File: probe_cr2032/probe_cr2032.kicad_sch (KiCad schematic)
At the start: 20 parts, among them J0 R0, U1 MCP73831-2-OT, U2 LTC3525-5, U3 MCP102-240D

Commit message: - add lasr fix
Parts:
- removed 5V1, 5V2, GND1, GND2: (no value), TestPoint:TestPoint_Pad_D1.5mm, symbol Connector:TestPoint
- removed C3: C1uF, Resistor_SMD:R_0603_1608Metric, symbol Device:C
- removed C4: C22uF, Resistor_SMD:R_0603_1608Metric, symbol Device:C
- removed J0: R0, Resistor_SMD:R_0201_0603Metric, symbol Device:R
- removed L1: 10UH, Inductor_SMD:L_Vishay_IFSC-1515AH_4x4x1.8mm, symbol Device:L
- removed U2: LTC3525-5, Package_TO_SOT_SMD:SOT-363_SC-70-6, symbol Regulator_Switching:LTC3525-5
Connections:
- net +5V: no longer names the net of C1.1, POW1.2 (A), U1.4 (VDD), USBC1.A9 (VBUS), USBC1.B9 (VBUS)

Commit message: - add new power version
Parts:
- removed U3: MCP102-240D, Package_TO_SOT_SMD:SOT-23, symbol Power_Supervisor:MCP100-270D
- added J?: Conn_01x03, Connector_Molex:Molex_CLIK-Mate_502386-0370_1x03-1MP_P1.25mm_Horizontal, symbol Connector_Generic:Conn_01x03
- added U?: APX809-23SAG-7, Package_TO_SOT_SMD:SOT-23, symbol 2025-03-20_10-07-06:APX809-23SAG-7
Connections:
- net GND: now also J?.3 (Pin_3), U?.1 (GND)
- net at C2.1, U1.3 (VBAT): now also J?.1 (Pin_1), U?.3 (VCC)
- net at LOW1.1: now also J?.2 (Pin_2), U?.2 (*RESET)
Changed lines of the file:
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@@
   (junction (at 156.21 72.39) (diameter 0) (color 0 0 0 0)
   )
+  (junction (at 204.47 85.09) (diameter 0) (color 0 0 0 0)
+  )
   (junction (at 111.76 67.31) (diameter 0) (color 0 0 0 0)
   )
@@
     (stroke (width 0) (type default) (color 0 0 0 0))
   )
-  (wire (pts (xy 186.69 95.25) (xy 186.69 97.79))
+  (wire (pts (xy 227.33 80.01) (xy 227.33 64.77))
+    (stroke (width 0) (type default) (color 0 0 0 0))
+  )
+  (wire (pts (xy 186.69 147.32) (xy 186.69 149.86))
     (stroke (width 0) (type default) (color 0 0 0 0))
   )
@@
     (stroke (width 0) (type default) (color 0 0 0 0))
   )
+  (wire (pts (xy 227.33 82.55) (xy 219.71 82.55))
+    (stroke (width 0) (type default) (color 0 0 0 0))
+  )
   (wire (pts (xy 60.96 67.31) (xy 60.96 109.22))
     (stroke (width 0) (type default) (color 0 0 0 0))
@@
     (stroke (width 0) (type default) (color 0 0 0 0))
   )
-  (wire (pts (xy 186.69 72.39) (xy 186.69 74.93))
+  (wire (pts (xy 186.69 72.39) (xy 186.69 86.36))
     (stroke (width 0) (type default) (color 0 0 0 0))
   )
@@
     (stroke (width 0) (type default) (color 0 0 0 0))
   )
+  (wire (pts (xy 227.33 64.77) (xy 165.1 64.77))
+    (stroke (width 0) (type default) (color 0 0 0 0))
+  )
   (wire (pts (xy 165.1 72.39) (xy 186.69 72.39))
     (stroke (width 0) (type default) (color 0 0 0 0))
@@
     (stroke (width 0) (type default) (color 0 0 0 0))
   )
+  (wire (pts (xy 189.23 86.36) (xy 189.23 85.09))
+    (stroke (width 0) (type default) (color 0 0 0 0))
+  )
+  (wire (pts (xy 226.06 85.09) (xy 226.06 88.9))
+    (stroke (width 0) (type default) (color 0 0 0 0))
+  )
+  (wire (pts (xy 204.47 85.09) (xy 219.71 85.09))
+    (stroke (width 0) (type default) (color 0 0 0 0))
+  )
+  (wire (pts (xy 189.23 85.09) (xy 204.47 85.09))
+    (stroke (width 0) (type default) (color 0 0 0 0))
+  )
+  (wire (pts (xy 227.33 85.09) (xy 226.06 85.09))
+    (stroke (width 0) (type default) (color 0 0 0 0))
+  )
   (wire (pts (xy 149.86 93.98) (xy 149.86 97.79))
     (stroke (width 0) (type default) (color 0 0 0 0))
   )
+  (wire (pts (xy 165.1 64.77) (xy 165.1 72.39))
+    (stroke (width 0) (type default) (color 0 0 0 0))
+  )
   (wire (pts (xy 135.89 77.47) (xy 139.7 77.47))
     (stroke (width 0) (type default) (color 0 0 0 0))
@@
     (stroke (width 0) (type default) (color 0 0 0 0))
   )
-  (wire (pts (xy 196.85 85.09) (xy 204.47 85.09))
-    (stroke (width 0) (type default) (color 0 0 0 0))
-  )
   (wire (pts (xy 165.1 80.01) (xy 165.1 97.79))
     (stroke (width 0) (type default) (color 0 0 0 0))
@@
     (stroke (width 0) (type default) (color 0 0 0 0))
   )
+  (wire (pts (xy 219.71 82.55) (xy 219.71 85.09))
+    (stroke (width 0) (type default) (color 0 0 0 0))
+  )
   (wire (pts (xy 147.32 67.31) (xy 111.76 67.31))
     (stroke (width 0) (type default) (color 0 0 0 0))
@@
     (pin "1")
     (pin "2")
+  )
+  (symbol (lib_id "Connector_Generic:Conn_01x03") (at 232.41 82.55 0) (unit 1)
+    (in_bom yes) (on_board yes) (fields_autoplaced)
+    (property "Reference" "J?" (id 0) (at 234.95 81.2799 0)
+      (effects (font (size 1.27 1.27)) (justify left))
+    )
+    (property "Value" "Conn_01x03" (id 1) (at 234.95 83.8199 0)
+      (effects (font (size 1.27 1.27)) (justify left))
+    )
+    (property "Footprint" "Connector_Molex:Molex_CLIK-Mate_502386-0370_1x03-1MP_P1.25mm_Horizontal" (id 2) (at 232.41 82.55 0)
+      (effects (font (size 1.27 1.27)) hide)
+    )
+    (property "Datasheet" "~" (id 3) (at 232.41 82.55 0)
+      (effects (font (size 1.27 1.27)) hide)
+    )
+    (pin "1")
+    (pin "2")
+    (pin "3")
   )
   (symbol (lib_id "power:GND") (at 111.76 97.79 0) (unit 1)
@@
     (pin "1")
   )
-  (symbol (lib_id "Power_Supervisor:MCP100-270D") (at 189.23 85.09 0) (unit 1)
-    (in_bom yes) (on_board yes)
-    (property "Reference" "U3" (id 0) (at 190.5 76.2 0)
-      (effects (font (size 1.27 1.27)) (justify right))
-    )
-    (property "Value" "MCP102-240D" (id 1) (at 201.93 95.25 0)
-      (effects (font (size 1.27 1.27)) (justify right))
-    )
-    (property "Footprint" "Package_TO_SOT_SMD:SOT-23" (id 2) (at 179.07 81.28 0)
-      (effects (font (size 1.27 1.27)) hide)
-    )
-    (property "Datasheet" "http://ww1.microchip.com/downloads/en/DeviceDoc/11187f.pdf" (id 3) (at 181.61 78.74 0)
-      (effects (font (size 1.27 1.27)) hide)
-    )
-    (pin "1")
-    (pin "2")
-    (pin "3")
-  )
   (symbol (lib_id "BATT:BAT") (at 165.1 76.2 270) (unit 1)
     (in_bom yes) (on_board yes)
-    (property "Reference" "CR02032" (id 0) (at 160.02 67.31 90)
+    (property "Reference" "CR02032" (id 0) (at 168.91 74.93 90)
       (effects (font (size 1.524 1.524)) (justify left))
     )
-    (property "Value" "BAT" (id 1) (at 162.56 69.85 90)
+    (property "Value" "BAT" (id 1) (at 171.45 77.47 90)
       (effects (font (size 1.524 1.524)) (justify left))
     )
@@
     (pin "1")
     (pin "2")
+  )
+  (symbol (lib_id "power:GND") (at 226.06 88.9 0) (unit 1)
+    (in_bom yes) (on_board yes) (fields_autoplaced)
+    (property "Reference" "#PWR?" (id 0) (at 226.06 95.25 0)
+      (effects (font (size 1.27 1.27)) hide)
+    )
+    (property "Value" "GND" (id 1) (at 226.06 93.98 0))
+    (property "Footprint" "" (id 2) (at 226.06 88.9 0)
+      (effects (font (size 1.27 1.27)) hide)
+    )
+    (property "Datasheet" "" (id 3) (at 226.06 88.9 0)
+      (effects (font (size 1.27 1.27)) hide)
+    )
+    (pin "1")
   )
   (symbol (lib_id "power:GND") (at 149.86 97.79 0) (unit 1)
@@
     (pin "1")
   )
-  (symbol (lib_id "power:GND") (at 186.69 97.79 0) (unit 1)
-    (in_bom yes) (on_board yes) (fields_autoplaced)
-    (property "Reference" "#PWR013" (id 0) (at 186.69 104.14 0)
-      (effects (font (size 1.27 1.27)) hide)
-    )
-    (property "Value" "GND" (id 1) (at 186.69 102.87 0))
-    (property "Footprint" "" (id 2) (at 186.69 97.79 0)
-      (effects (font (size 1.27 1.27)) hide)
-    )
-    (property "Datasheet" "" (id 3) (at 186.69 97.79 0)
+  (symbol (lib_id "power:GND") (at 186.69 149.86 0) (unit 1)
+    (in_bom yes) (on_board yes) (fields_autoplaced)
+    (property "Reference" "#PWR013" (id 0) (at 186.69 156.21 0)
+      (effects (font (size 1.27 1.27)) hide)
+    )
+    (property "Value" "GND" (id 1) (at 186.69 154.94 0))
+    (property "Footprint" "" (id 2) (at 186.69 149.86 0)
+      (effects (font (size 1.27 1.27)) hide)
+    )
+    (property "Datasheet" "" (id 3) (at 186.69 149.86 0)
       (effects (font (size 1.27 1.27)) hide)
     )
@@
     (pin "2")
   )
+  (symbol (lib_id "2025-03-20_10-07-06:APX809-23SAG-7") (at 186.69 147.32 90) (unit 1)
+    (in_bom yes) (on_board yes) (fields_autoplaced)
+    (property "Reference" "U?" (id 0) (at 195.58 115.57 90)
+      (effects (font (size 1.524 1.524)) (justify right))
+    )
+    (property "Value" "APX809-23SAG-7" (id 1) (at 195.58 119.38 90)
+      (effects (font (size 1.524 1.524)) (justify right))
+    )
+    (property "Footprint" "Package_TO_SOT_SMD:SOT-23" (id 2) (at 180.594 116.84 0)
+      (effects (font (size 1.524 1.524)) hide)
+    )
+    (property "Datasheet" "" (id 3) (at 186.69 147.32 0)
+      (effects (font (size 1.524 1.524)))
+    )
+    (pin "1")
+    (pin "2")
+    (pin "3")
+  )
   (symbol (lib_id "Device:R") (at 132.08 77.47 270) (unit 1)
     (in_bom yes) (on_board yes)
@@
       (reference "#PWR014") (unit 1) (value "GND") (footprint "")
     )
+    (path "/5c96ba60-7a3e-4c72-82fa-4dd4553921d5"
+      (reference "#PWR?") (unit 1) (value "GND") (footprint "")
+    )
     (path "/d84ac55d-e98a-478c-a252-de5af85c069f"
       (reference "C1") (unit 1) (value "C4.7uF") (footprint "Resistor_SMD:R_0603_1608Metric")
@@
       (reference "CR02032") (unit 1) (value "BAT") (footprint "Battery:BatteryHolder_MPD_BC2003_1x2032")
     )
+    (path "/0b1fdd35-21c8-40ab-84f6-dd033fb97a89"
+      (reference "J?") (unit 1) (value "Conn_01x03") (footprint "Connector_Molex:Molex_CLIK-Mate_502386-0370_1x03-1MP_P1.25mm_Horizontal")
+    )
     (path "/efb5de02-294a-4d48-b323-8ca668cb19c2"
       (reference "LOW1") (unit 1) (value " ") (footprint "TestPoint:TestPoint_Pad_D1.5mm")
@@
       (reference "U1") (unit 1) (value "MCP73831-2-OT") (footprint "Package_TO_SOT_SMD:SOT-23-5")
     )
-    (path "/27d3c657-b334-46f1-b2a3-dcb6f71c4942"
-      (reference "U3") (unit 1) (value "MCP102-240D") (footprint "Package_TO_SOT_SMD:SOT-23")
+    (path "/d9599d89-f7d1-4bd1-b21d-3d78018df852"
+      (reference "U?") (unit 1) (value "APX809-23SAG-7") (footprint "Package_TO_SOT_SMD:SOT-23")
     )
     (path "/7ff708b3-b7ff-412b-835f-9670901eb122"

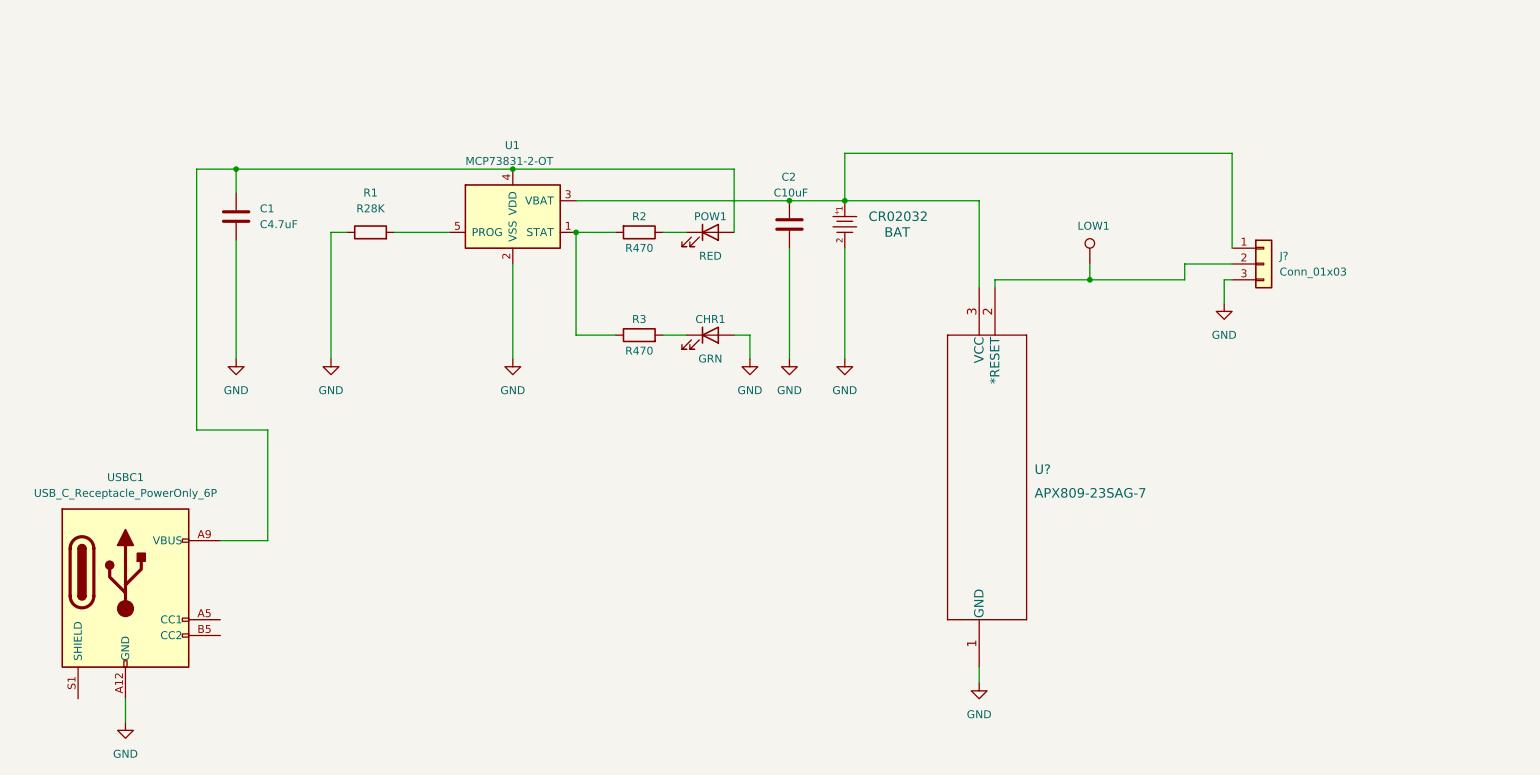
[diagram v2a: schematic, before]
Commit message: - add new probe_cr_2032
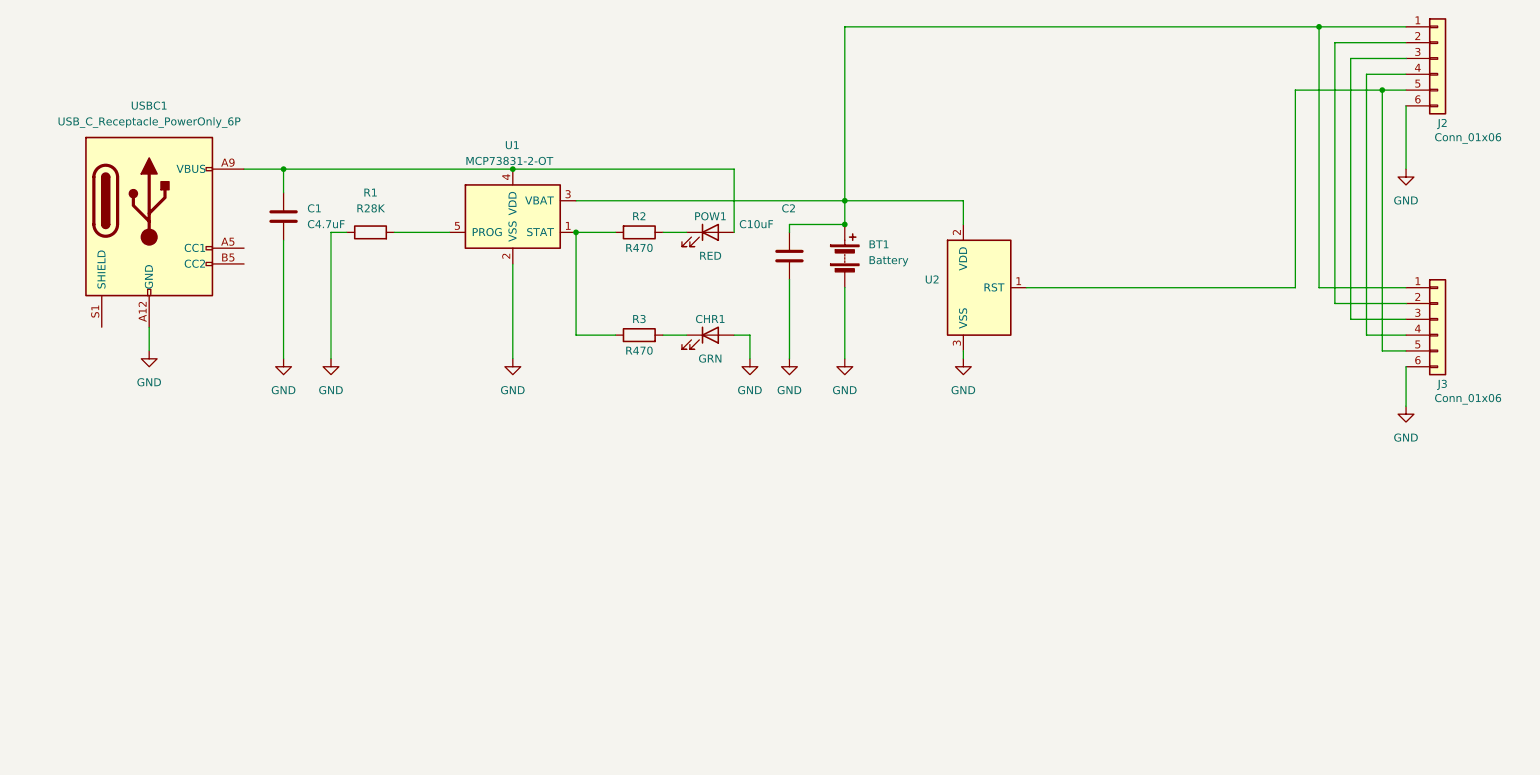
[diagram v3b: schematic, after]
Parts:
- removed J?: Conn_01x03, Connector_Molex:Molex_CLIK-Mate_502386-0370_1x03-1MP_P1.25mm_Horizontal, symbol Connector_Generic:Conn_01x03
- removed LOW1: (no value), TestPoint:TestPoint_Pad_D1.5mm, symbol Connector:TestPoint
- removed U?: APX809-23SAG-7, Package_TO_SOT_SMD:SOT-23, symbol 2025-03-20_10-07-06:APX809-23SAG-7
- added BT1: Battery, Battery:BatteryHolder_MPD_BC2003_1x2032, symbol Device:Battery
- added J2, J3: Conn_01x06, Connector_FFC-FPC:TE_0-1734839-6_1x06-1MP_P0.5mm_Horizontal, symbol Connector_Generic:Conn_01x06
- added U2: MCP101-300D, Package_TO_SOT_SMD:SOT-23, symbol Power_Supervisor:MCP101-300D
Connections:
- net GND: now also BT1.2 (-), J2.6 (Pin_6), J3.6 (Pin_6), U2.3 (VSS)
- net at C2.1, U1.3 (VBAT): now also BT1.1 (+), J2.1 (Pin_1), J3.1 (Pin_1), U2.2 (VDD)
- new net: J2.2 (Pin_2), J3.2 (Pin_2)
- new net: J2.3 (Pin_3), J3.3 (Pin_3)
- new net: J2.4 (Pin_4), J3.4 (Pin_4)
- new net: J2.5 (Pin_5), J3.5 (Pin_5), U2.1 (RST)
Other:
- moved on the sheet: C1, C2, USBC1

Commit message: -add last fix for attinty84
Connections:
- net GND: now also CHR1.1 (K); no longer CHR1.2 (A)
- net at R3.2: now also CHR1.2 (A); no longer CHR1.1 (K)
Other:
- moved on the sheet: CHR1
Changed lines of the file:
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@@
 	(symbol
 		(lib_id "Device:LED")
-		(at 143.51 93.98 0)
+		(at 143.51 93.98 180)
 		(unit 1)
 		(exclude_from_sim no)
@@
 		(dnp no)
 		(property "Reference" "CHR1"
-			(at 143.51 91.44 0)
+			(at 143.51 96.52 0)
 			(effects
 				(font
@@
 		)
 		(property "Value" "GRN"
-			(at 143.51 97.79 0)
+			(at 143.51 90.17 0)
 			(effects
 				(font
